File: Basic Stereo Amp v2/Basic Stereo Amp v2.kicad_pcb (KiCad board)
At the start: 2 copper layers, 100 x 100 mm, 78 parts, among them J1 Conn_Coaxial_x2, J2 Screw_Terminal_01x02, J3 Screw_Terminal_01x04, J4 AudioJack3, J5 Barrel_Jack_Switch, Q1 NJVMJB42CT4G, Q2 NJVMJB41CT4G, Q3 NJVMJB42CT4G, Q4 NJVMJB41CT4G, Q5 DMP6180SK3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

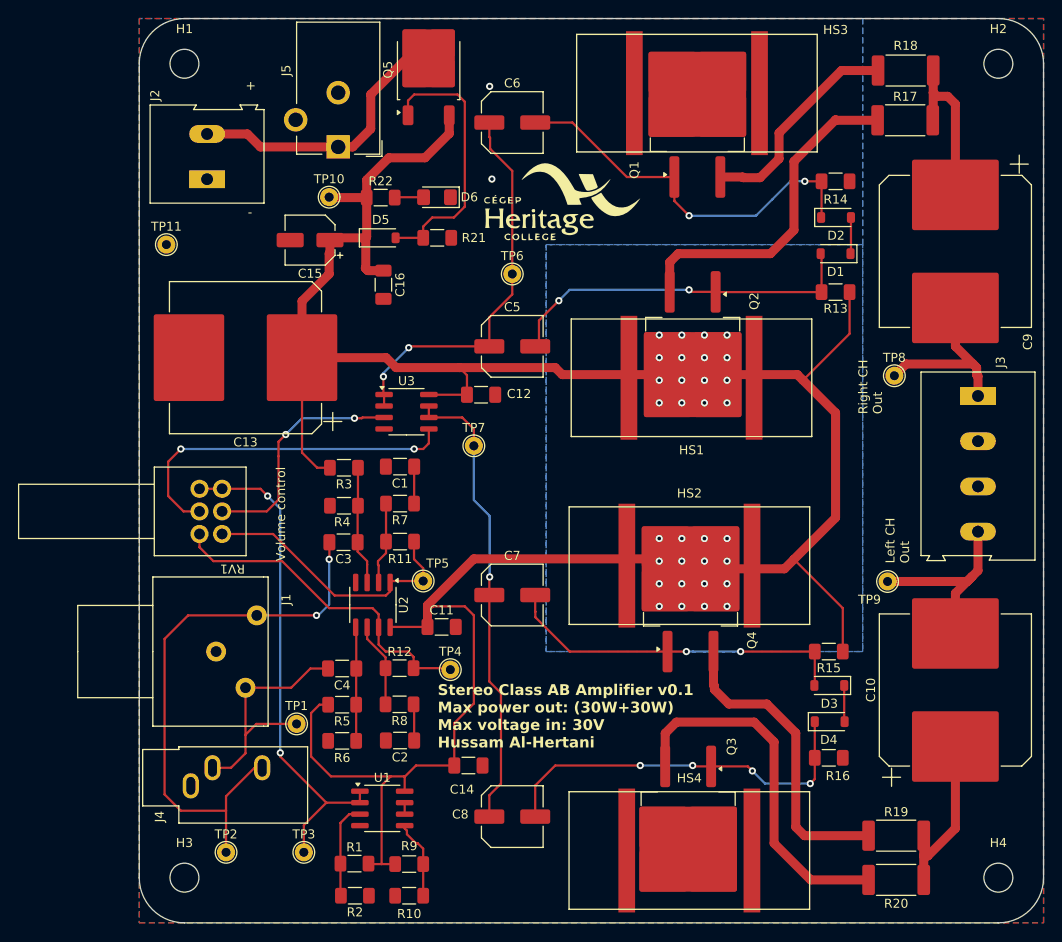
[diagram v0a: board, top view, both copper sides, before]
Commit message: Added16 Channel Servo controller Design
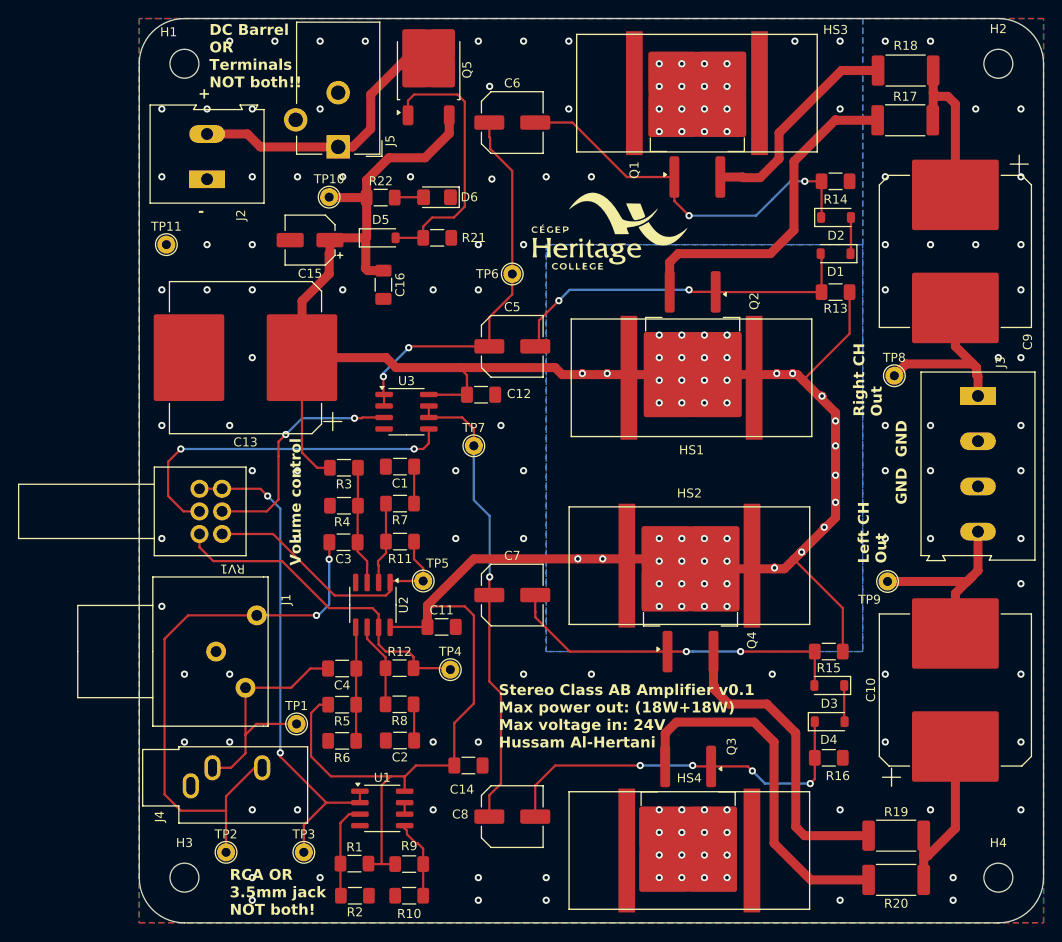
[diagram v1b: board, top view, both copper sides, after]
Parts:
- moved G*** 6.17 mm to (151.8, 73.5)
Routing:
- net VCC: track 291.1 -> 291.9 mm, vias 32 -> 46
- net GND: vias 2 -> 132
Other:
- board text added: "DC Barrel OR Terminals NOT both!!"
- board text added: "GND GND"
- board text added: "RCA OR 3.5mm jack NOT both!"
- board text added: "Stereo Class AB Amplifier v0.1 Max power out: (18W+18W) Max voltage in: 24V Hussam Al-Hertani"
- board text removed: "Stereo Class AB Amplifier v0.1 Max power out: (30W+30W) Max voltage in: 30V Hussam Al-Hertani"

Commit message: latest updates as of Oct 2nd 2024
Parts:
- moved TP6 3.26 mm to (138.0, 78.0)
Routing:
- net Net-(D1-A): track 40.1 -> 46.1 mm, vias 2 -> 0
- net Net-(D2-K): track 43.1 -> 38.4 mm
- net Net-(D3-A): track 38.7 -> 43.4 mm, vias 2 -> 0
- net Net-(U3A--): track 43.5 -> 42.0 mm
- net GND: vias 132 -> 124
